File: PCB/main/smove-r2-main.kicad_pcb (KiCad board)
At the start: 4 copper layers, 25 x 35 mm, 36 parts, among them J1 TYPE-C-31-M-12, J2 PH2 protected pack, J3 UART 3V3 / DNF, J4 PH4 to carrier, SW2 RESET, SW3 BOOT / USER, U1 ESP32-C3-MINI-1-N4, U4 AP2112K-3.3TRG1, U6 BQ24074RGTR, U8 USBLC6-2SC6, U9 PESD5V0S2BT,215

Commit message: Split main schematic into wired USB Power Compute sheets and document IMU housing alignment
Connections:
- net /BOOT renamed /Compute/BOOT
- net /CC1 renamed /USB/CC1
- net /CC2 renamed /USB/CC2
- net /CHG_ILIM renamed /Power/CHG_ILIM
- net /CHG_ISET renamed /Power/CHG_ISET
- net /LED_B renamed /Compute/LED_B
- net /LED_B_K renamed /Compute/LED_B_K
- net /LED_G renamed /Compute/LED_G
- net /LED_G_K renamed /Compute/LED_G_K
- net /LED_R renamed /Compute/LED_R
- net /LED_R_K renamed /Compute/LED_R_K
- net /MCU_EN renamed /Compute/MCU_EN
- net /PACK_P renamed /Power/PACK_P
- net /SCL_HOST renamed /Compute/SCL_HOST
- net /SDA_HOST renamed /Compute/SDA_HOST
- net /STRAP2 renamed /Compute/STRAP2
- net /STRAP8 renamed /Compute/STRAP8
- net /SYS renamed /Power/SYS
- net /TS_NO_CELL_SENSING renamed /Power/TS_NO_CELL_SENSING
- net /UART_RX renamed /Compute/UART_RX
- net /UART_TX renamed /Compute/UART_TX
- net /USB_DM_MCU renamed /Compute/USB_DM_MCU
- net /USB_DP_MCU renamed /Compute/USB_DP_MCU

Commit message: Add ESP32 BOOT and RESET silkscreen labels and verification artifacts
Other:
- board text added: "BOOT"
- board text added: "RESET"
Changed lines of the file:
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@@
 	)
 	(embedded_fonts no)
+	(gr_text "RESET"
+		(at 110.2 123.7 90)
+		(layer "F.SilkS")
+		(effects (font (size 0.8 0.8) (thickness 0.15)))
+	)
+	(gr_text "BOOT"
+		(at 110.2 130 90)
+		(layer "F.SilkS")
+		(effects (font (size 0.8 0.8) (thickness 0.15)))
+	)
 )

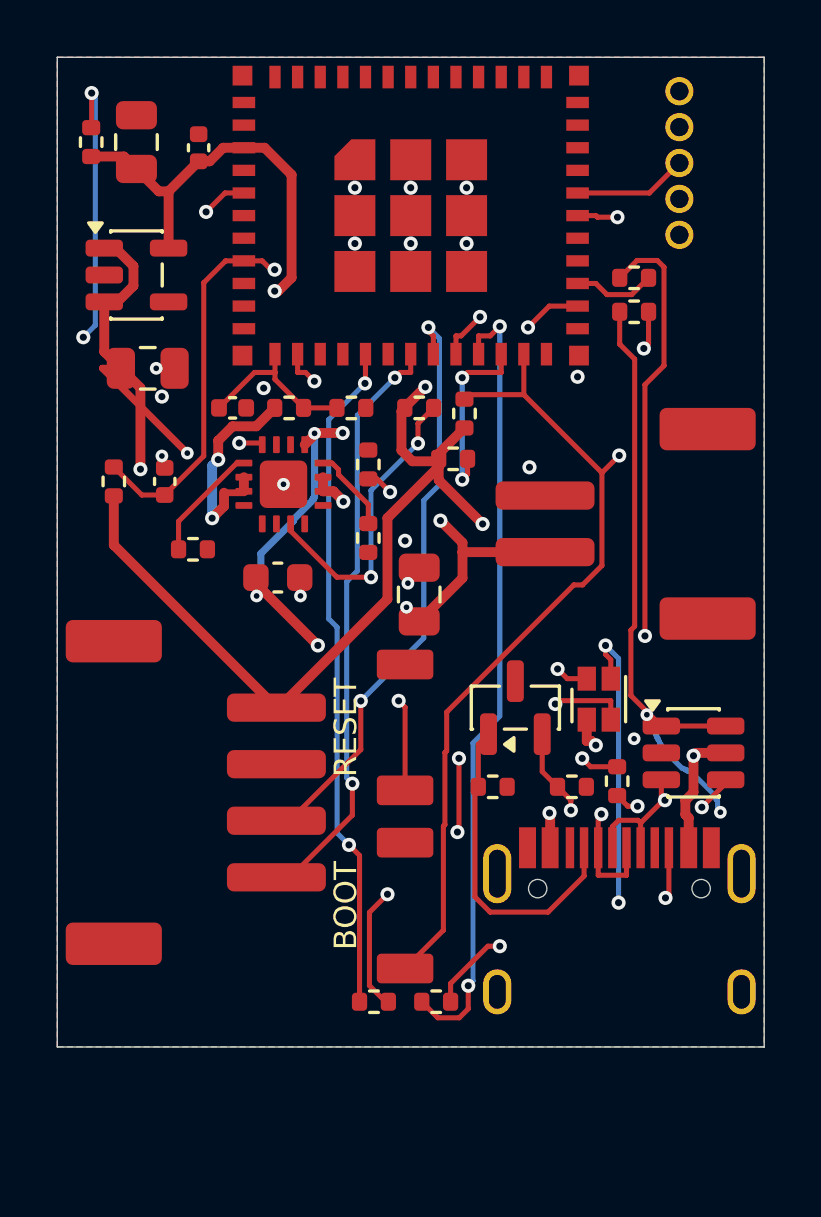
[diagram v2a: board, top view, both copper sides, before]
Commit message: Recover compact native delivery from preserved autostash and hash-matched objects
Explicitly commit all 142 recovery paths (51 restored tracked modifications, 91 additions including recovered assets and forensic verification evidence). Preserve the original 30 merged paths unchanged. Do not apply the historical unused-footprint deletion.

Restore exact compact PCB/schematics/FCStd/source/export bytes; all 138 delivery-manifest entries match. Fresh electrical 1214/1214, source/export coherence 657/657, mechanical 2087/2088 with original conservative PH2 reservation gate retained; 7 groups and 58 individual links independently movable.

Original 152-path staging index is unavailable: preserve all 1004 initially unreachable objects, record pathname confidence, and do not claim proven recovery of every original pathname. GUI casing launch remains blocked by desktop lock screen. No merge, redesign, deletion or advisor activity.
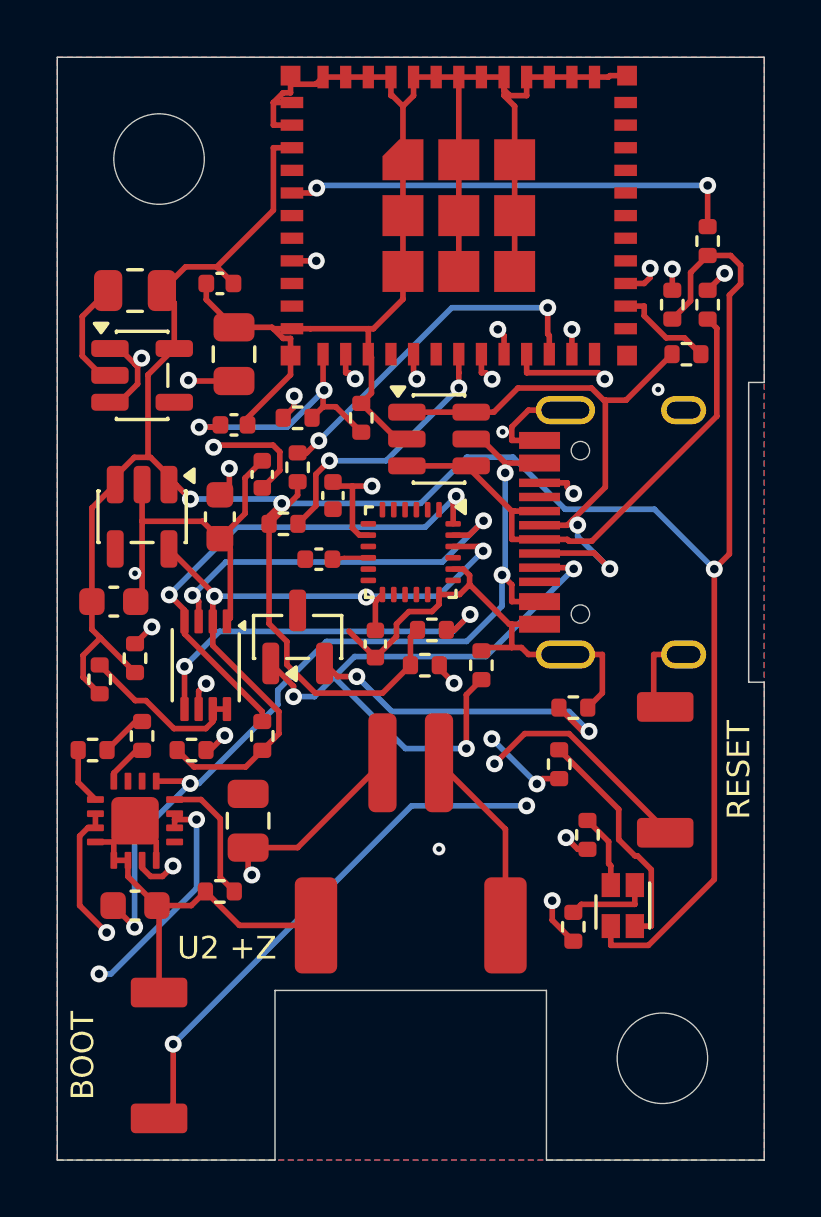
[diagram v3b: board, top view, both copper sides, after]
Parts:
- removed J3: UART 3V3 / DNF, smove-r2-main:Debug_5
- removed J4: PH4 to carrier, smove-r2-main:JST_PH_S4B-PH-SM4-TB_1x04-1MP_P2.00mm_Horizontal
- added C5: 4.7u / 16V X5R, imu:C_0603_1608Metric, F.Cu at (102.0, 119.2)
- added C6: 4.7u / 16V X5R, imu:C_0603_1608Metric, F.Cu at (105.8, 116.2)
- added C7: 100n / 16V, imu:C_0402_1005Metric, F.Cu at (111.2, 120.8)
- added C8: 100n / 16V, imu:C_0402_1005Metric, F.Cu at (109.8, 115.5)
- added C9: 100n / 16V, imu:C_0402_1005Metric, F.Cu at (109.2, 117.8)
- added H1: M3 NPTH 3.2mm, MountingHole_3.2mm_M3, F.Cu at (103.6, 103.6)
- added H2: M3 NPTH 3.2mm, MountingHole_3.2mm_M3, F.Cu at (121.4, 135.4)
- added R16: 4.7k 1%, imu:R_0402_1005Metric, F.Cu at (104.8, 124.5)
- added R17: 4.7k 1%, imu:R_0402_1005Metric, F.Cu at (107.2, 124.0)
- added R18: 4.7k 1%, imu:R_0402_1005Metric, F.Cu at (108.0, 116.5)
- added R19: 4.7k 1%, imu:R_0402_1005Metric, F.Cu at (113.2, 120.2)
- added R20: 200k 1%, imu:R_0402_1005Metric, F.Cu at (101.5, 122.0)
- added U2: ICM-20948, imu:InvenSense_QFN-24_3x3mm_P0.4mm, F.Cu at (112.5, 117.5)
- added U3: PCA9306DCUR, imu:PCA9306_DCU0008A, F.Cu at (105.2, 121.5)
- added U5: AP2112K-1.8TRG1, imu:SOT-23-5, F.Cu at (103.0, 116.2)
- moved R9 22.1 mm to (123.0, 106.5)
- moved J1 15.2 mm to (121.1, 116.8), turned to 90 degrees
- moved U8 14.3 mm to (113.5, 113.5)
- moved J2 13.6 mm to (112.5, 127.8), turned to 0 degrees
- moved R22 13.6 mm to (105.8, 129.5), turned to 180 degrees
- moved U6 13.0 mm to (102.8, 127.0)
- moved C1 12.7 mm to (102.8, 130.0)
- moved R21 12.5 mm to (103.0, 124.0)
- moved R13 10.7 mm to (117.8, 125.0), turned to 90 degrees
- moved SW3 10.2 mm to (103.6, 135.3)
- moved C2 10.0 mm to (106.8, 127.0)
- moved SW2 9.32 mm to (121.5, 125.2)
- moved R5 9.10 mm to (113.0, 121.5)
- moved R8 8.30 mm to (121.8, 108.8)
- moved U9 8.10 mm to (108.5, 120.5)
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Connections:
- net /Compute/BOOT renamed Net-(U1-GPIO9_/_BOOT)
- U1 pad 18: /Compute/SCL_HOST -> /SCL_HOST
- U1 pad 19: /Compute/SDA_HOST -> /SDA_HOST
- U1 pad 30: /Compute/UART_RX -> unconnected-(U1-GPIO20_/_RX-Pad30)
- U1 pad 31: /Compute/UART_TX -> unconnected-(U1-GPIO21_/_TX-Pad31)
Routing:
- net GND: track 1.98 -> 123.0 mm, vias 17 -> 4
- net /IMU/1V8_IMU: track 0.00 -> 39.0 mm, vias 0 -> 5
- net /3V3_MAIN: track 62.0 -> 96.4 mm, vias 4 -> 3
- net /SDA_HOST: track 0.00 -> 23.3 mm, vias 0 -> 3
- net /VBUS: track 54.1 -> 32.1 mm, vias 6 -> 4
- net /Compute/SDA_HOST: track 21.3 -> 0.00 mm, vias 2 -> 0
- net /Compute/SCL_HOST: track 21.1 -> 0.00 mm, vias 2 -> 0
- net /IMU/SCL_1V8: track 0.00 -> 20.7 mm, vias 0 -> 3
- net /SCL_HOST: track 0.00 -> 20.2 mm, vias 0 -> 3
- net /IMU/SDA_1V8: track 0.00 -> 18.5 mm, vias 0 -> 2
- net /Compute/LED_G_K: track 18.3 -> 2.97 mm, vias 3 -> 0
- net /USB/CC2: track 9.57 -> 22.3 mm, vias 2 -> 3
- net /USB/CC1: track 11.6 -> 22.9 mm, vias 0 -> 3
- net /USB_DP: track 30.1 -> 19.1 mm, vias 3 -> 0
- net /USB_POWER_N: track 16.6 -> 27.6 mm
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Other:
- board size 25 x 35 mm -> 25 x 39 mm
- board text added: "BODY"
- board text added: "U2 +Z"
- board text removed: "sMove R2 MAIN PROTOTYPE"

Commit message: Compact PCB and housing with 2.54mm PTH battery wire pads
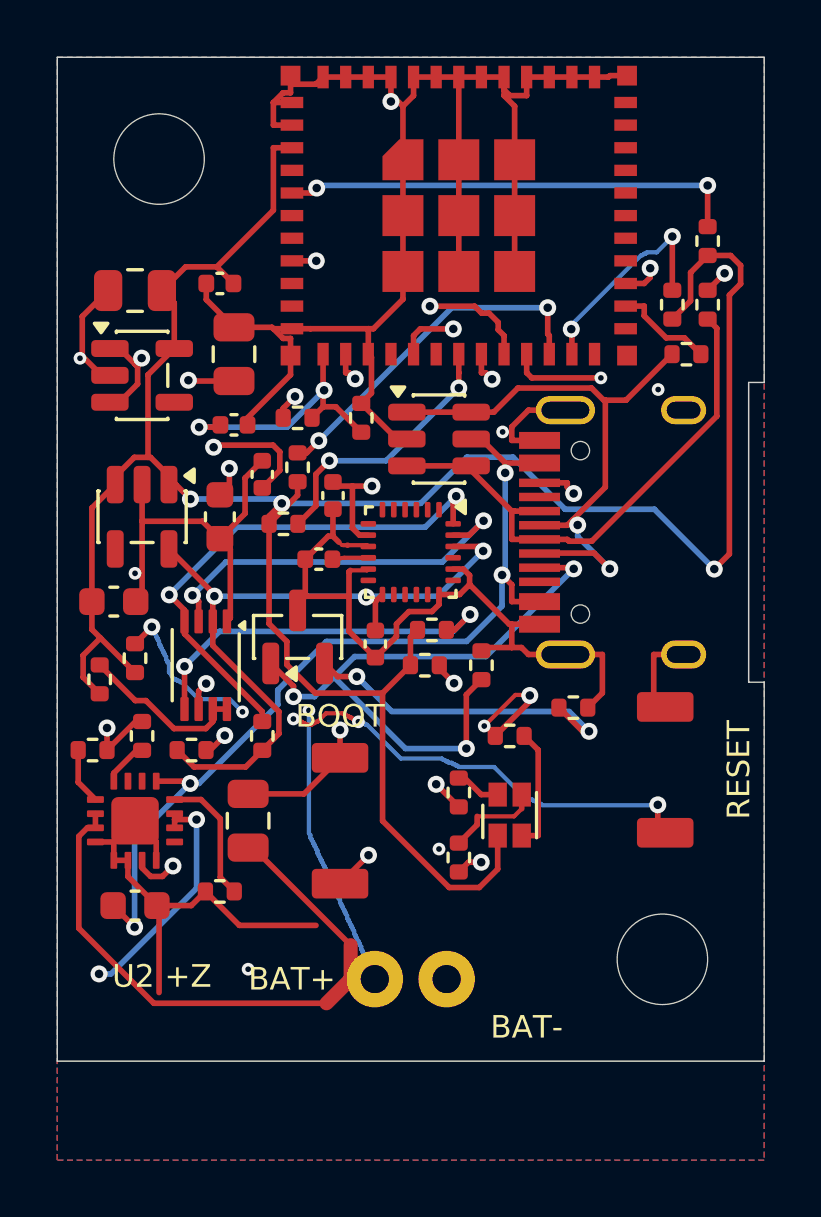
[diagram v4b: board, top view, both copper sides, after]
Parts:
- J2: value PH2 protected pack -> Battery wire pads 2.54mm; footprint smove-r2-main:JST_PH_S2B-PH-SM4-TB_1x02-1MP_P2.00mm_Horizontal -> smove-r2-main:BatteryWire_2x_PTH_P2.54mm_D1.0mm
- moved SW3 10.5 mm to (110.0, 127.0)
- moved D1 5.12 mm to (116.0, 126.8)
- moved J2 4.80 mm to (112.5, 132.6)
- moved R11 4.79 mm to (114.2, 126.0)
- moved R12 4.73 mm to (114.2, 128.3)
- moved H2 3.50 mm to (121.4, 131.9)
- moved R13 2.02 mm to (116.0, 124.0), turned to 0 degrees
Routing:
- net Net-(U1-GPIO9_/_BOOT): track 42.6 -> 31.2 mm, vias 4 -> 3
- net GND: track 123.0 -> 131.9 mm, vias 4 -> 9
- net /Power/PACK_P: track 39.8 -> 46.4 mm, vias 3 -> 2
- net /Compute/MCU_EN: track 49.9 -> 43.8 mm, vias 4 -> 7
- net /3V3_MAIN: track 96.4 -> 91.1 mm
- net /Compute/LED_B_K: track 8.22 -> 4.31 mm
- net /Compute/LED_B: track 17.9 -> 21.0 mm
- net /Compute/LED_G: track 25.1 -> 23.7 mm
- net /Compute/LED_R: track 21.8 -> 23.0 mm
- net /Compute/LED_R_K: track 2.63 -> 1.62 mm
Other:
- board size 25 x 39 mm -> 25 x 35.5 mm
- board text added: "BAT+"
- board text added: "BAT-"
